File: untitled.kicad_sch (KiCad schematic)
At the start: 10 parts, among them J1 Conn_01x02_Pin, U1 LM2596S-5, U2 LM1117DT-3.3

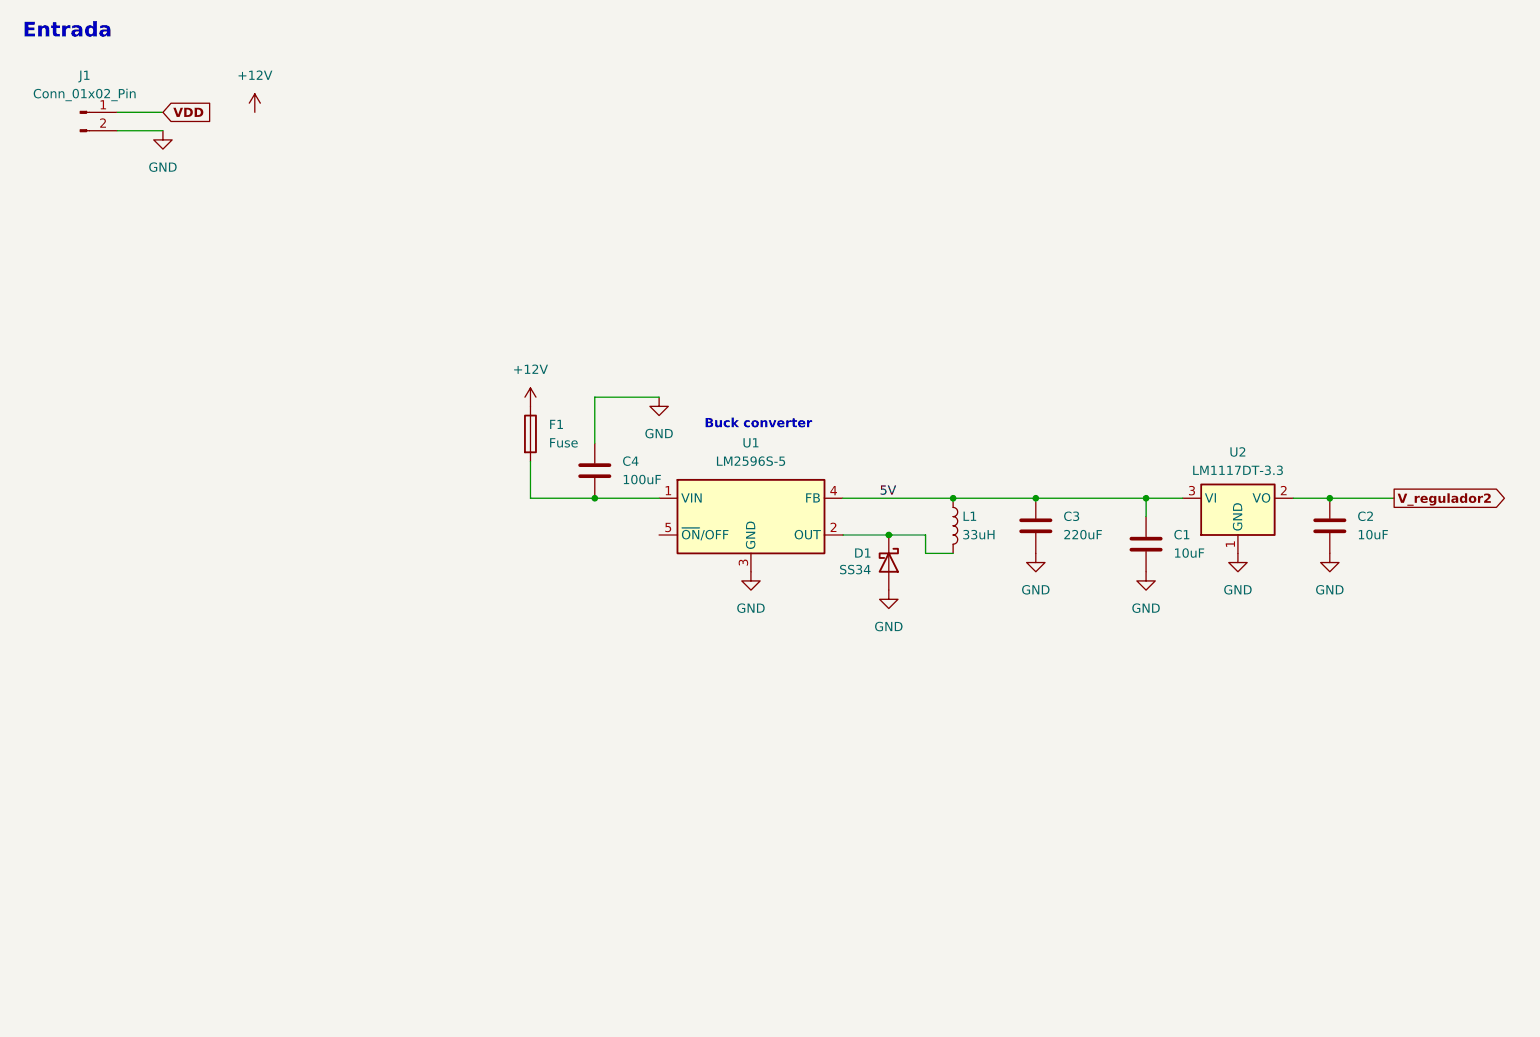
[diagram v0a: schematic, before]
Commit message: Actualització projecte KiCad
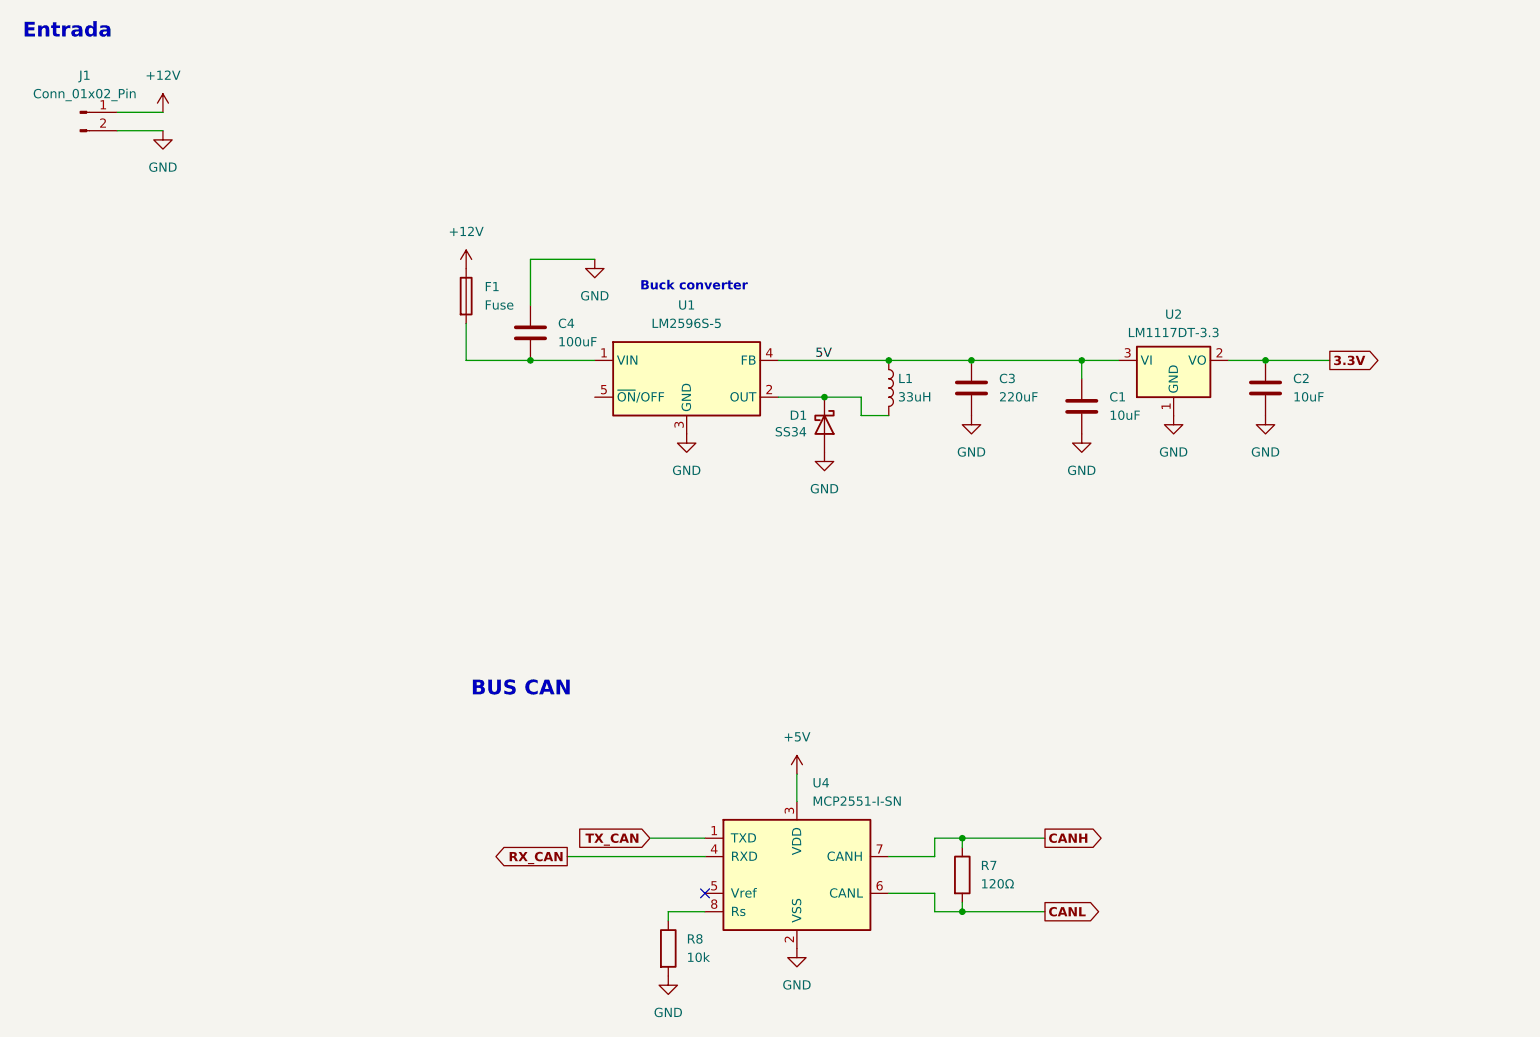
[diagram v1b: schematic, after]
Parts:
- added R7: 120Ω, symbol Device:R
- added R8: 10k, symbol Device:R
- added U4: MCP2551-I-SN, Package_SO:SOIC-8_3.9x4.9mm_P1.27mm, symbol Interface_CAN_LIN:MCP2551-I-SN
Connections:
- net VDD is gone; now on net +12V: J1.1 (Pin_1)
- net GND: now also R8.2, U4.2 (VSS)
- net V_regulador2 renamed 3.3V
- new net: R8.1, U4.8 (Rs)
- new net +5V: U4.3 (VDD)
- new net CANH: R7.1, U4.7 (CANH)
- new net CANL: R7.2, U4.6 (CANL)
- new net RX_CAN: U4.4 (RXD)
- new net TX_CAN: U4.1 (TXD)
- no-connect marks 0 -> 1
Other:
- note added: "BUS CAN"
- moved on the sheet: C1, C2, C3, C4, D1, F1, L1, U1, U2
